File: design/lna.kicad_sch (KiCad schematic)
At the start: 22 parts, among them J5 SMA, U9 ADA4930-1

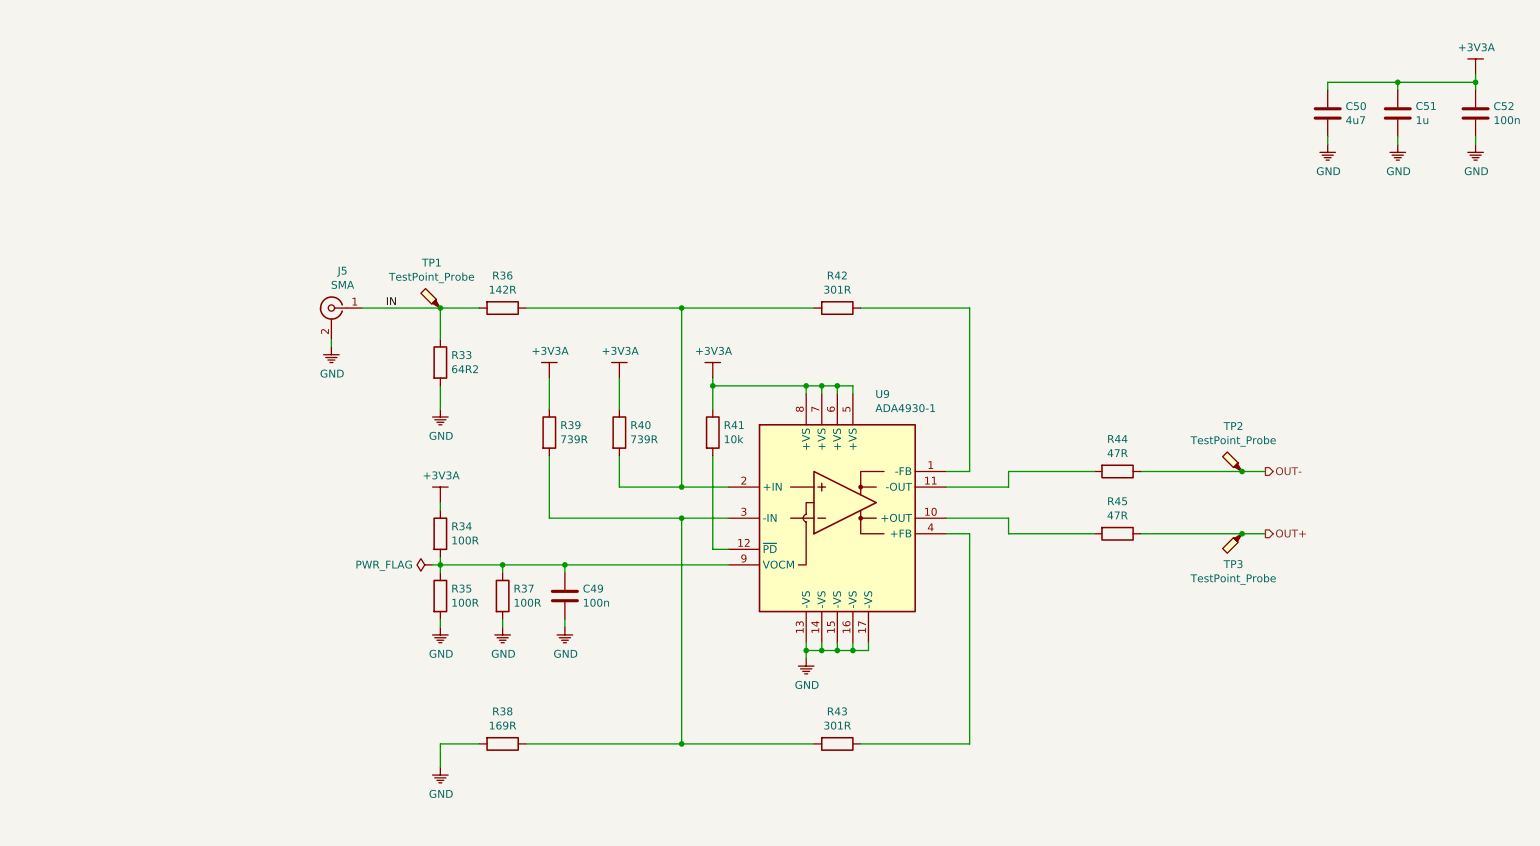
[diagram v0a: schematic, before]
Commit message: Removed LNA test points
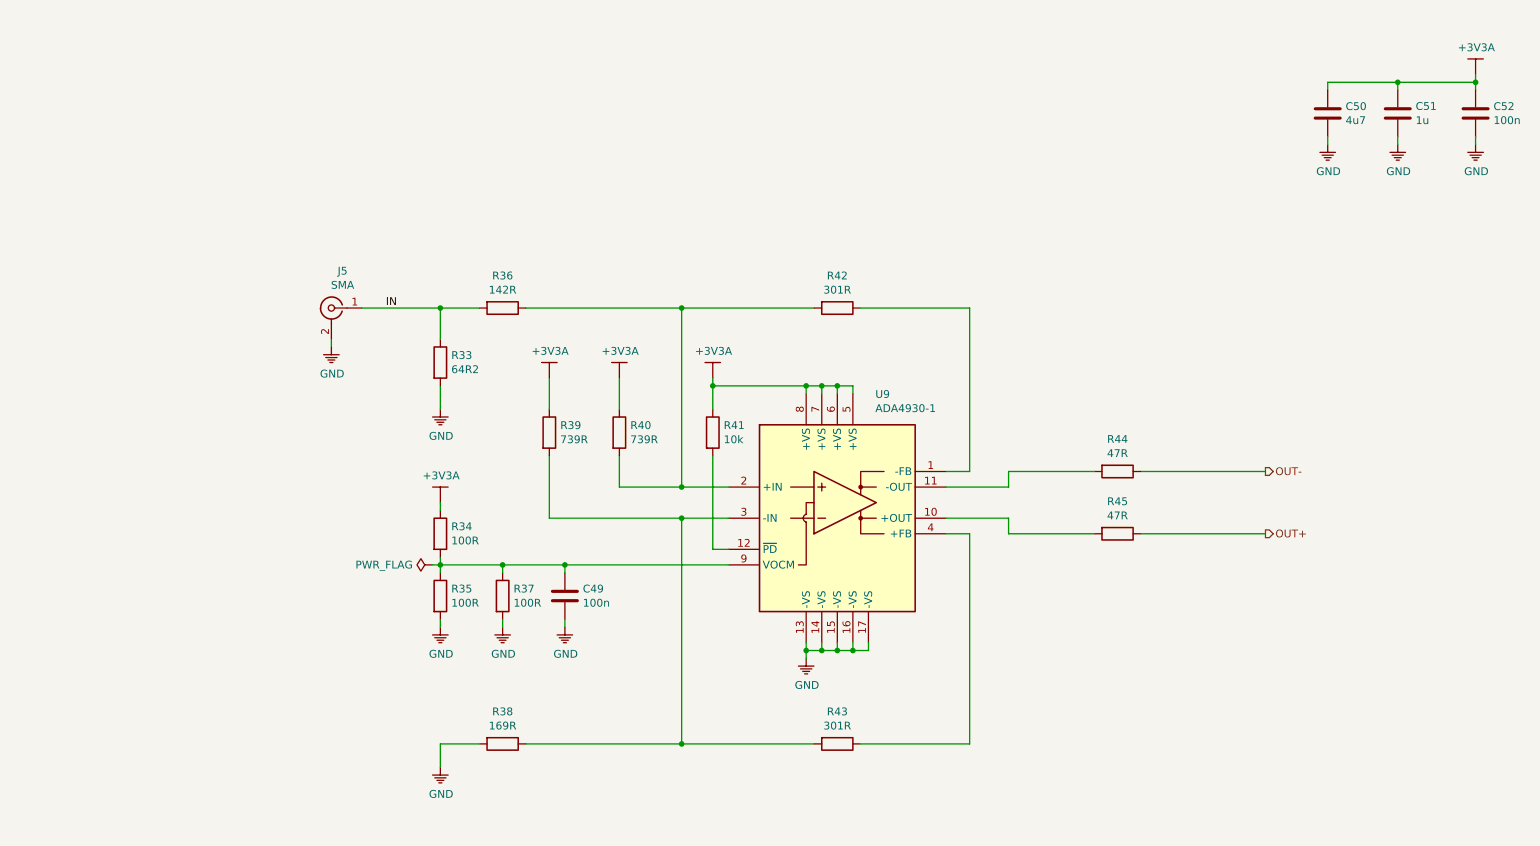
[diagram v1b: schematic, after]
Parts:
- removed TP1, TP2, TP3: TestPoint_Probe, TestPoint:TestPoint_Pad_D1.0mm, symbol Connector:TestPoint_Probe
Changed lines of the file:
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@@
 (kicad_sch (version 20200512) (host eeschema "5.99.0-unknown-d72a778~101~ubuntu18.04.1")
-  (page 1 8)
+  (page 5 8)
   (paper "A4")
   (title_block
@@
   (junction (at 149.86 119.38))
   (junction (at 152.4 119.38))
-  (junction (at 215.9 90.17))
-  (junction (at 215.9 100.33))
   (junction (at 241.3 26.67))
   (junction (at 254 26.67))
@@
   (wire (pts (xy 177.8 97.79) (xy 177.8 100.33)))
   (wire (pts (xy 177.8 100.33) (xy 191.77 100.33)))
-  (wire (pts (xy 199.39 90.17) (xy 215.9 90.17)))
-  (wire (pts (xy 199.39 100.33) (xy 215.9 100.33)))
-  (wire (pts (xy 215.9 90.17) (xy 219.71 90.17)))
-  (wire (pts (xy 219.71 100.33) (xy 215.9 100.33)))
+  (wire (pts (xy 199.39 90.17) (xy 219.71 90.17)))
+  (wire (pts (xy 199.39 100.33) (xy 219.71 100.33)))
   (wire (pts (xy 229.87 26.67) (xy 229.87 27.94)))
   (wire (pts (xy 229.87 26.67) (xy 241.3 26.67)))
@@
       (effects (font (size 1.27 1.27)) hide)
     )
-  )
-  (symbol (lib_id "Connector:TestPoint_Probe") (at 85.09 63.5 90) (unit 1)
-    (property "Reference" "TP1" (id 0) (at 83.693 56.134 90))
-    (property "Value" "TestPoint_Probe" (id 1) (at 83.693 58.4454 90))
-    (property "Footprint" "TestPoint:TestPoint_Pad_D1.0mm" (id 2) (at 85.09 58.42 0)
-      (effects (font (size 1.27 1.27)) hide)
-    )
-    (property "Datasheet" "~" (id 3) (at 85.09 58.42 0)
-      (effects (font (size 1.27 1.27)) hide)
-    )
-  )
-  (symbol (lib_id "Connector:TestPoint_Probe") (at 215.9 90.17 90) (unit 1)
-    (property "Reference" "TP2" (id 0) (at 214.503 82.804 90))
-    (property "Value" "TestPoint_Probe" (id 1) (at 214.503 85.1154 90))
-    (property "Footprint" "TestPoint:TestPoint_Pad_D1.0mm" (id 2) (at 215.9 85.09 0)
-      (effects (font (size 1.27 1.27)) hide)
-    )
-    (property "Datasheet" "~" (id 3) (at 215.9 85.09 0)
-      (effects (font (size 1.27 1.27)) hide)
-    )
-  )
-  (symbol (lib_id "Connector:TestPoint_Probe") (at 215.9 100.33 180) (unit 1)
-    (property "Reference" "TP3" (id 0) (at 214.503 105.3338 0))
-    (property "Value" "TestPoint_Probe" (id 1) (at 214.503 107.6452 0))
-    (property "Footprint" "TestPoint:TestPoint_Pad_D1.0mm" (id 2) (at 210.82 100.33 0)
-      (effects (font (size 1.27 1.27)) hide)
-    )
-    (property "Datasheet" "~" (id 3) (at 210.82 100.33 0)
-      (effects (font (size 1.27 1.27)) hide)
-    )

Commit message: Updated some layout
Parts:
- renumbered C49 to C53, C50 to C54, C51 to C55, C52 to C56, R33 to R36, R34 to R37, R35 to R38, R36 to R39, R37 to R40, R38 to R41, R39 to R42, R40 to R43, R41 to R44, R42 to R45, R43 to R46, R44 to R47, R45 to R48, U9 to U10
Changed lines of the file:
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@@
   )
   (symbol (lib_id "KLIB_Power:GND") (at 67.31 69.85 0) (unit 1)
-    (property "Reference" "#PWR097" (id 0) (at 67.31 74.93 0)
+    (property "Reference" "#PWR0108" (id 0) (at 67.31 74.93 0)
       (effects (font (size 1.27 1.27)) hide)
     )
@@
   )
   (symbol (lib_id "KLIB_Power:GND") (at 85.09 80.01 0) (unit 1)
-    (property "Reference" "#PWR098" (id 0) (at 85.09 85.09 0)
+    (property "Reference" "#PWR0109" (id 0) (at 85.09 85.09 0)
       (effects (font (size 1.27 1.27)) hide)
     )
@@
   )
   (symbol (lib_id "KLIB_Power:+3V3A") (at 85.09 95.25 0) (unit 1)
-    (property "Reference" "#PWR099" (id 0) (at 85.09 102.87 0)
+    (property "Reference" "#PWR0110" (id 0) (at 85.09 102.87 0)
       (effects (font (size 1.27 1.27)) hide)
     )
@@
   )
   (symbol (lib_id "KLIB_Power:GND") (at 85.09 115.57 0) (unit 1)
-    (property "Reference" "#PWR0100" (id 0) (at 85.09 120.65 0)
+    (property "Reference" "#PWR0111" (id 0) (at 85.09 120.65 0)
       (effects (font (size 1.27 1.27)) hide)
     )
@@
   )
   (symbol (lib_id "KLIB_Power:GND") (at 85.09 138.43 0) (unit 1)
-    (property "Reference" "#PWR0101" (id 0) (at 85.09 143.51 0)
+    (property "Reference" "#PWR0112" (id 0) (at 85.09 143.51 0)
       (effects (font (size 1.27 1.27)) hide)
     )
@@
   )
   (symbol (lib_id "KLIB_Power:GND") (at 95.25 115.57 0) (unit 1)
-    (property "Reference" "#PWR0102" (id 0) (at 95.25 120.65 0)
+    (property "Reference" "#PWR0113" (id 0) (at 95.25 120.65 0)
       (effects (font (size 1.27 1.27)) hide)
     )
@@
   )
   (symbol (lib_id "KLIB_Power:+3V3A") (at 102.87 74.93 0) (unit 1)
-    (property "Reference" "#PWR0103" (id 0) (at 102.87 82.55 0)
+    (property "Reference" "#PWR0114" (id 0) (at 102.87 82.55 0)
       (effects (font (size 1.27 1.27)) hide)
     )
@@
   )
   (symbol (lib_id "KLIB_Power:GND") (at 105.41 115.57 0) (unit 1)
-    (property "Reference" "#PWR0104" (id 0) (at 105.41 120.65 0)
+    (property "Reference" "#PWR0115" (id 0) (at 105.41 120.65 0)
       (effects (font (size 1.27 1.27)) hide)
     )
@@
   )
   (symbol (lib_id "KLIB_Power:+3V3A") (at 114.3 74.93 0) (unit 1)
-    (property "Reference" "#PWR0105" (id 0) (at 114.3 82.55 0)
+    (property "Reference" "#PWR0116" (id 0) (at 114.3 82.55 0)
       (effects (font (size 1.27 1.27)) hide)
     )
@@
   )
   (symbol (lib_id "KLIB_Power:+3V3A") (at 129.54 74.93 0) (unit 1)
-    (property "Reference" "#PWR0139" (id 0) (at 129.54 82.55 0)
+    (property "Reference" "#PWR0117" (id 0) (at 129.54 82.55 0)
       (effects (font (size 1.27 1.27)) hide)
     )
@@
   )
   (symbol (lib_id "KLIB_Power:GND") (at 144.78 120.65 0) (unit 1)
-    (property "Reference" "#PWR0106" (id 0) (at 144.78 125.73 0)
+    (property "Reference" "#PWR0118" (id 0) (at 144.78 125.73 0)
       (effects (font (size 1.27 1.27)) hide)
     )
@@
   )
   (symbol (lib_id "KLIB_Power:GND") (at 229.87 36.83 0) (unit 1)
-    (property "Reference" "#PWR0107" (id 0) (at 229.87 41.91 0)
+    (property "Reference" "#PWR0119" (id 0) (at 229.87 41.91 0)
       (effects (font (size 1.27 1.27)) hide)
     )
@@
   )
   (symbol (lib_id "KLIB_Power:GND") (at 241.3 36.83 0) (unit 1)
-    (property "Reference" "#PWR0108" (id 0) (at 241.3 41.91 0)
+    (property "Reference" "#PWR0120" (id 0) (at 241.3 41.91 0)
       (effects (font (size 1.27 1.27)) hide)
     )
@@
   )
   (symbol (lib_id "KLIB_Power:+3V3A") (at 254 25.4 0) (unit 1)
-    (property "Reference" "#PWR0109" (id 0) (at 254 33.02 0)
+    (property "Reference" "#PWR0121" (id 0) (at 254 33.02 0)
       (effects (font (size 1.27 1.27)) hide)
     )
@@
   )
   (symbol (lib_id "KLIB_Power:GND") (at 254 36.83 0) (unit 1)
-    (property "Reference" "#PWR0110" (id 0) (at 254 41.91 0)
+    (property "Reference" "#PWR0122" (id 0) (at 254 41.91 0)
       (effects (font (size 1.27 1.27)) hide)
     )
@@
   )
   (symbol (lib_id "Device:R") (at 85.09 72.39 0) (unit 1)
-    (property "Reference" "R33" (id 0) (at 86.868 71.2216 0)
+    (property "Reference" "R36" (id 0) (at 86.868 71.2216 0)
       (effects (font (size 1.27 1.27)) (justify left))
     )
@@
   )
   (symbol (lib_id "Device:R") (at 85.09 100.33 0) (unit 1)
-    (property "Reference" "R34" (id 0) (at 86.868 99.1616 0)
+    (property "Reference" "R37" (id 0) (at 86.868 99.1616 0)
       (effects (font (size 1.27 1.27)) (justify left))
     )
@@
   )
   (symbol (lib_id "Device:R") (at 85.09 110.49 0) (unit 1)
-    (property "Reference" "R35" (id 0) (at 86.868 109.3216 0)
+    (property "Reference" "R38" (id 0) (at 86.868 109.3216 0)
       (effects (font (size 1.27 1.27)) (justify left))
     )
@@
   )
   (symbol (lib_id "Device:R") (at 95.25 63.5 270) (unit 1)
-    (property "Reference" "R36" (id 0) (at 95.25 58.2422 90))
+    (property "Reference" "R39" (id 0) (at 95.25 58.2422 90))
     (property "Value" "142R" (id 1) (at 95.25 60.5536 90))
     (property "Footprint" "Resistor_SMD:R_0603_1608Metric" (id 2) (at 95.25 61.722 90)
@@
   )
   (symbol (lib_id "Device:R") (at 95.25 110.49 0) (unit 1)
-    (property "Reference" "R37" (id 0) (at 97.028 109.3216 0)
+    (property "Reference" "R40" (id 0) (at 97.028 109.3216 0)
       (effects (font (size 1.27 1.27)) (justify left))
     )
@@
   )
   (symbol (lib_id "Device:R") (at 95.25 134.62 270) (unit 1)
-    (property "Reference" "R38" (id 0) (at 95.25 129.3622 90))
+    (property "Reference" "R41" (id 0) (at 95.25 129.3622 90))
     (property "Value" "169R" (id 1) (at 95.25 131.6736 90))
     (property "Footprint" "Resistor_SMD:R_0603_1608Metric" (id 2) (at 95.25 132.842 90)
@@
   )
   (symbol (lib_id "Device:R") (at 102.87 83.82 0) (unit 1)
-    (property "Reference" "R39" (id 0) (at 104.648 82.6516 0)
+    (property "Reference" "R42" (id 0) (at 104.648 82.6516 0)
       (effects (font (size 1.27 1.27)) (justify left))
     )
@@
   )
   (symbol (lib_id "Device:R") (at 114.3 83.82 0) (unit 1)
-    (property "Reference" "R40" (id 0) (at 116.078 82.6516 0)
+    (property "Reference" "R43" (id 0) (at 116.078 82.6516 0)
       (effects (font (size 1.27 1.27)) (justify left))
     )
@@
   )
   (symbol (lib_id "Device:R") (at 129.54 83.82 0) (unit 1)
-    (property "Reference" "R41" (id 0) (at 131.318 82.6516 0)
+    (property "Reference" "R44" (id 0) (at 131.318 82.6516 0)
       (effects (font (size 1.27 1.27)) (justify left))
     )
@@
   )
   (symbol (lib_id "Device:R") (at 149.86 63.5 270) (unit 1)
-    (property "Reference" "R42" (id 0) (at 149.86 58.2422 90))
+    (property "Reference" "R45" (id 0) (at 149.86 58.2422 90))
     (property "Value" "301R" (id 1) (at 149.86 60.5536 90))
     (property "Footprint" "Resistor_SMD:R_0603_1608Metric" (id 2) (at 149.86 61.722 90)
@@
   )
   (symbol (lib_id "Device:R") (at 149.86 134.62 270) (unit 1)
-    (property "Reference" "R43" (id 0) (at 149.86 129.3622 90))
+    (property "Reference" "R46" (id 0) (at 149.86 129.3622 90))
     (property "Value" "301R" (id 1) (at 149.86 131.6736 90))
     (property "Footprint" "Resistor_SMD:R_0603_1608Metric" (id 2) (at 149.86 132.842 90)
@@
   )
   (symbol (lib_id "Device:R") (at 195.58 90.17 270) (unit 1)
-    (property "Reference" "R44" (id 0) (at 195.58 84.9122 90))
+    (property "Reference" "R47" (id 0) (at 195.58 84.9122 90))
     (property "Value" "47R" (id 1) (at 195.58 87.2236 90))
     (property "Footprint" "Resistor_SMD:R_0402_1005Metric" (id 2) (at 195.58 88.392 90)
@@
   )
   (symbol (lib_id "Device:R") (at 195.58 100.33 270) (unit 1)
-    (property "Reference" "R45" (id 0) (at 195.58 95.0722 90))
+    (property "Reference" "R48" (id 0) (at 195.58 95.0722 90))
     (property "Value" "47R" (id 1) (at 195.58 97.3836 90))
     (property "Footprint" "Resistor_SMD:R_0402_1005Metric" (id 2) (at 195.58 98.552 90)
@@
   )
   (symbol (lib_id "Device:C") (at 105.41 110.49 0) (unit 1)
-    (property "Reference" "C49" (id 0) (at 108.331 109.3216 0)
+    (property "Reference" "C53" (id 0) (at 108.331 109.3216 0)
       (effects (font (size 1.27 1.27)) (justify left))
     )
@@
   )
   (symbol (lib_id "Device:C") (at 229.87 31.75 0) (unit 1)
-    (property "Reference" "C50" (id 0) (at 232.791 30.607 0)
+    (property "Reference" "C54" (id 0) (at 232.791 30.607 0)
       (effects (font (size 1.27 1.27)) (justify left))
     )
@@
   )
   (symbol (lib_id "Device:C") (at 241.3 31.75 0) (unit 1)
-    (property "Reference" "C51" (id 0) (at 244.221 30.5816 0)
+    (property "Reference" "C55" (id 0) (at 244.221 30.5816 0)
       (effects (font (size 1.27 1.27)) (justify left))
     )
@@
   )
   (symbol (lib_id "Device:C") (at 254 31.75 0) (unit 1)
-    (property "Reference" "C52" (id 0) (at 256.921 30.607 0)
+    (property "Reference" "C56" (id 0) (at 256.921 30.607 0)
       (effects (font (size 1.27 1.27)) (justify left))
     )
@@
   )
   (symbol (lib_id "KLIB_Amplifier:ADA4930-1") (at 149.86 97.79 0) (unit 1)
-    (property "Reference" "U9" (id 0) (at 156.0576 77.5716 0)
-      (effects (font (size 1.27 1.27)) (justify left))
-    )
+    (property "Reference" "U10" (id 0) (at 156.0576 77.5716 0)
+      (effects (font (size 1.27 1.27)) (justify left))
+    )
